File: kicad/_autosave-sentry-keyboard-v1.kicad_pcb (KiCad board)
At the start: 2 copper layers, 315 x 121 mm, 269 parts, among them J2 Conn_01x04, J4 AVR-ISP-6, SW1 Reset, SW2 RotaryEncoder_Switch, U1 ATmega32U4-AU, Y1 16Mhz

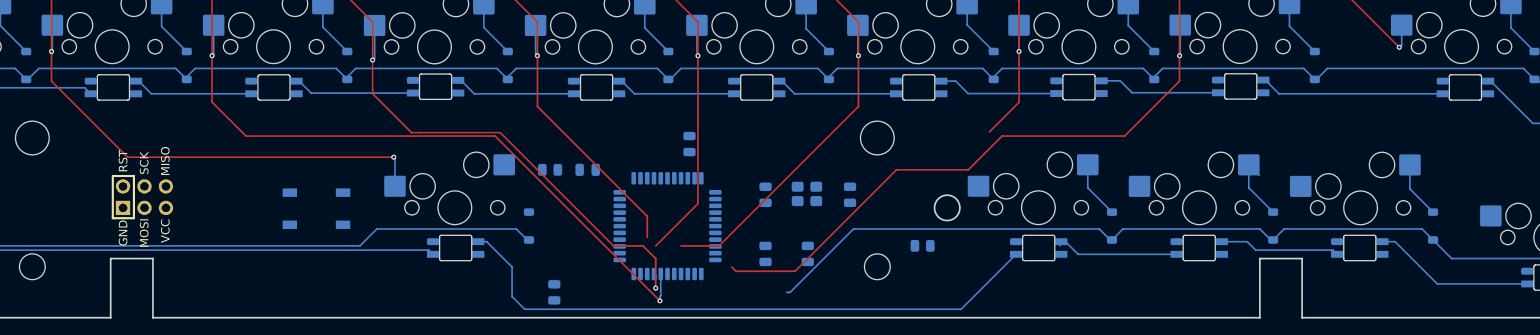
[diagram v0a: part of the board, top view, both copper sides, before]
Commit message: More routing progress
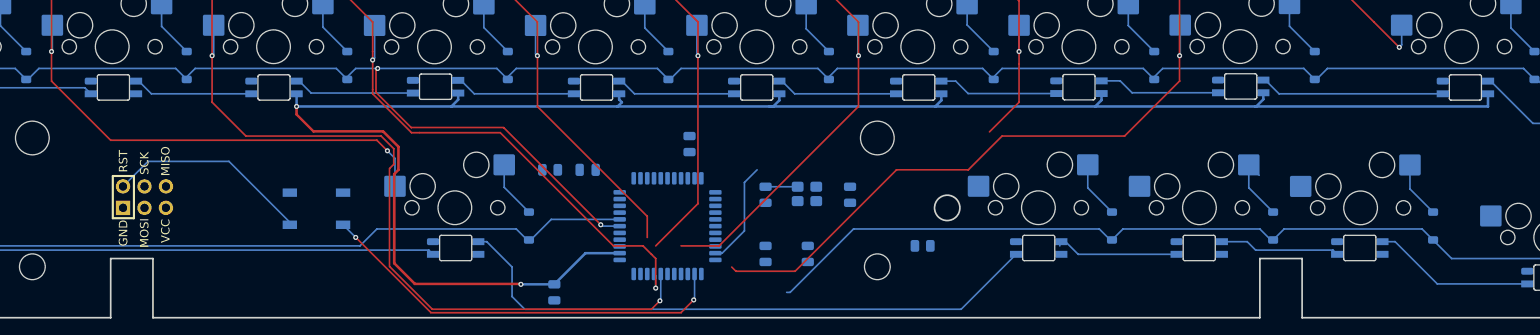
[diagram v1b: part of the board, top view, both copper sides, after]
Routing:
- net +5V: track 149.7 -> 363.2 mm, vias 0 -> 2
- net Net-(J4-~{RST}): track 0.00 -> 73.8 mm, vias 0 -> 2
- net Row4: track 349.6 -> 387.6 mm, vias 2 -> 4
- net Row2: track 271.4 -> 283.8 mm
- net Row5: track 269.3 -> 281.1 mm
- net Col4: track 181.5 -> 191.2 mm
- net Net-(D76-A): track 0.62 -> 7.43 mm
- net Net-(U1-XTAL2): track 0.00 -> 3.80 mm
